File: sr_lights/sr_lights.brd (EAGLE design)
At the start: 78.4 x 64.8 mm, 33 parts, among them T1 BC847, T2 BC847, T3 BC847, T4 BC847, T5 BC847, T6 BC847, T7 BC847, T8 BC847

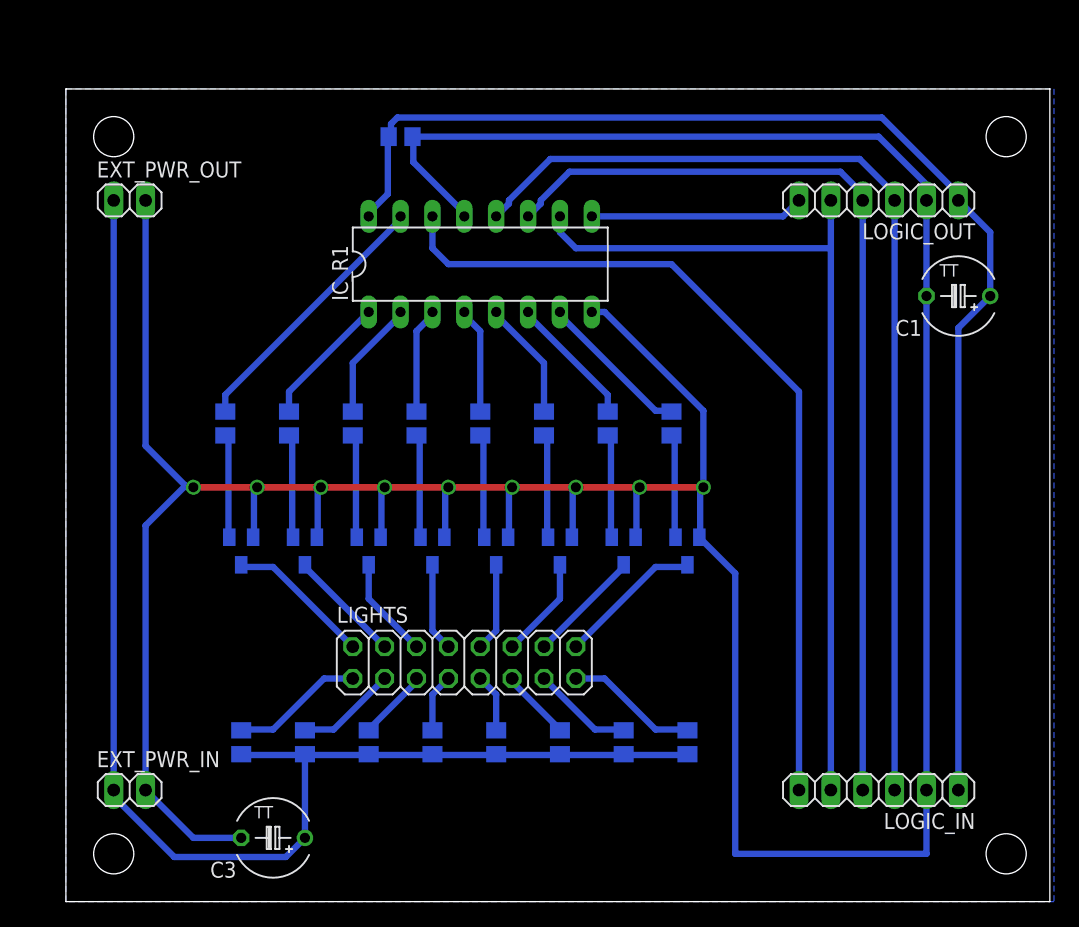
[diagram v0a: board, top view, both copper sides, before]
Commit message: DRC and align: Set the same DRC for lights and motors, fixed new DRC errors in sr_lights, aligned headers
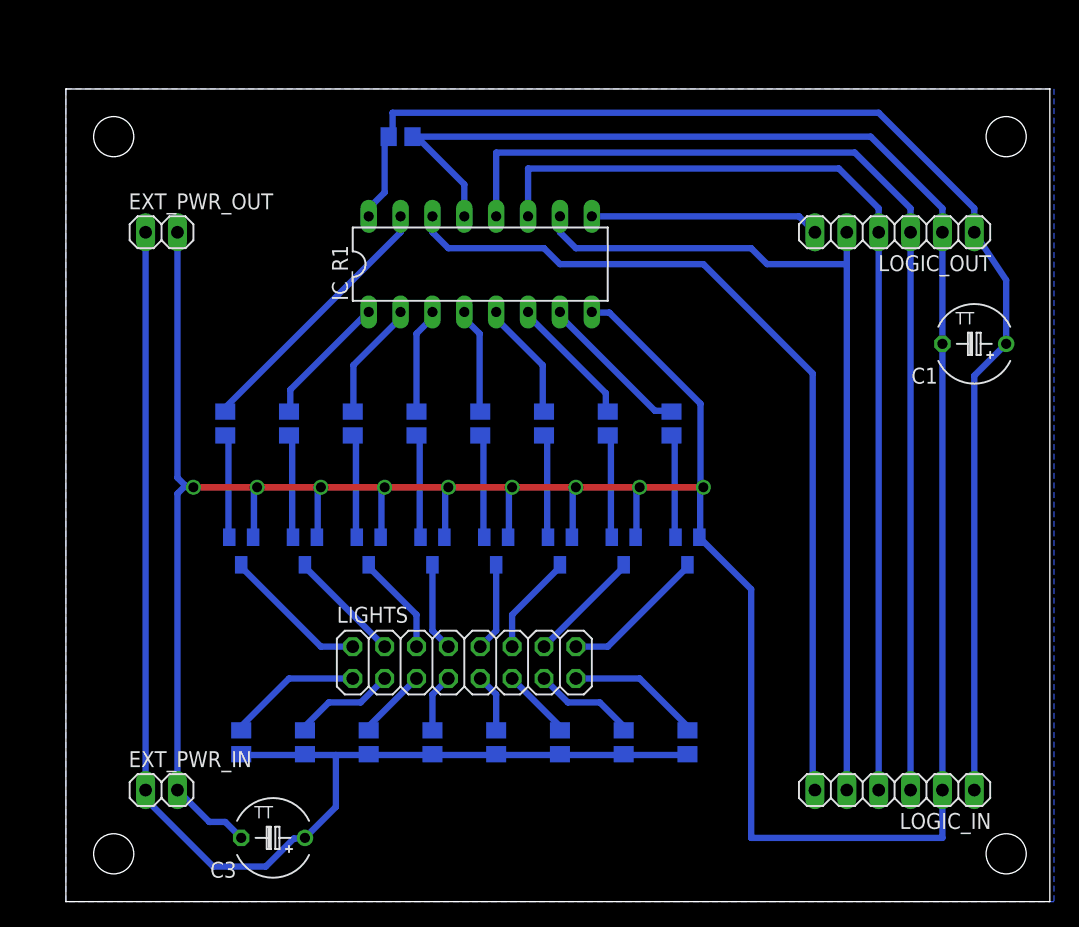
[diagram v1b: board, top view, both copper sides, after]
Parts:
- moved C1 4.02 mm to (72.4, 44.5)
- moved EXT_PWR_OUT 3.59 mm to (7.62, 53.3)
- moved LOGIC_OUT 2.84 mm to (66.0, 53.3)
- moved EXT_PWR_IN 2.54 mm to (7.62, 8.89)
- moved LOGIC_IN 1.27 mm to (66.0, 8.89)
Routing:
- net GND: track 297.9 -> 289.3 mm
- net RCK: track 82.4 -> 86.3 mm
- net VCC2: track 108.1 -> 104.7 mm
- net SCK: track 76.5 -> 79.4 mm
- net VCC1: track 105.8 -> 107.3 mm
- net SI0: track 68.2 -> 69.6 mm
- net SI1: track 17.0 -> 18.3 mm
- net SCLR: track 70.4 -> 69.5 mm

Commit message: Verion 1.2: Increased route width and board width, small other changes
Squashed commit of the following:

commit cb5b4ae53fc73325e271569d8207a4f4cb0d995e
Author: Sergey Kostyuk <contact@s-kostyuk.me>
Date:   Tue Sep 13 19:34:33 2016 +0300

    Increaded width of routes, increased board width, replaced capacitor package, updated board version

commit 30ef558f6f82cadcaf764826f9decc7df1a17ce0
Author: Sergey Kostyuk <contact@s-kostyuk.me>
Date:   Tue Sep 13 19:27:19 2016 +0300

    Replaced capacitor package

commit a2d398c50457a8d09da237926f830a1984b8064b
Author: Sergey Kostyuk <contact@s-kostyuk.me>
Date:   Tue Sep 13 18:08:38 2016 +0300

    Icreased width of routes, icreased board width

commit f5951c6459f5b93fe179c3fabd85f49e6b5260dd
Author: Sergey Kostyuk <contact@s-kostyuk.me>
Date:   Wed Sep 7 16:51:49 2016 +0300

    Increased width of power lines on sr_motors

commit 1e2f38b3539c2f4abccb8c8183ef937e4e63213c
Author: Sergey Kostyuk <ks.hot.ua@gmail.com>
Date:   Mon Aug 22 15:17:33 2016 +0300

    Added reverse current protection for external power, added version text
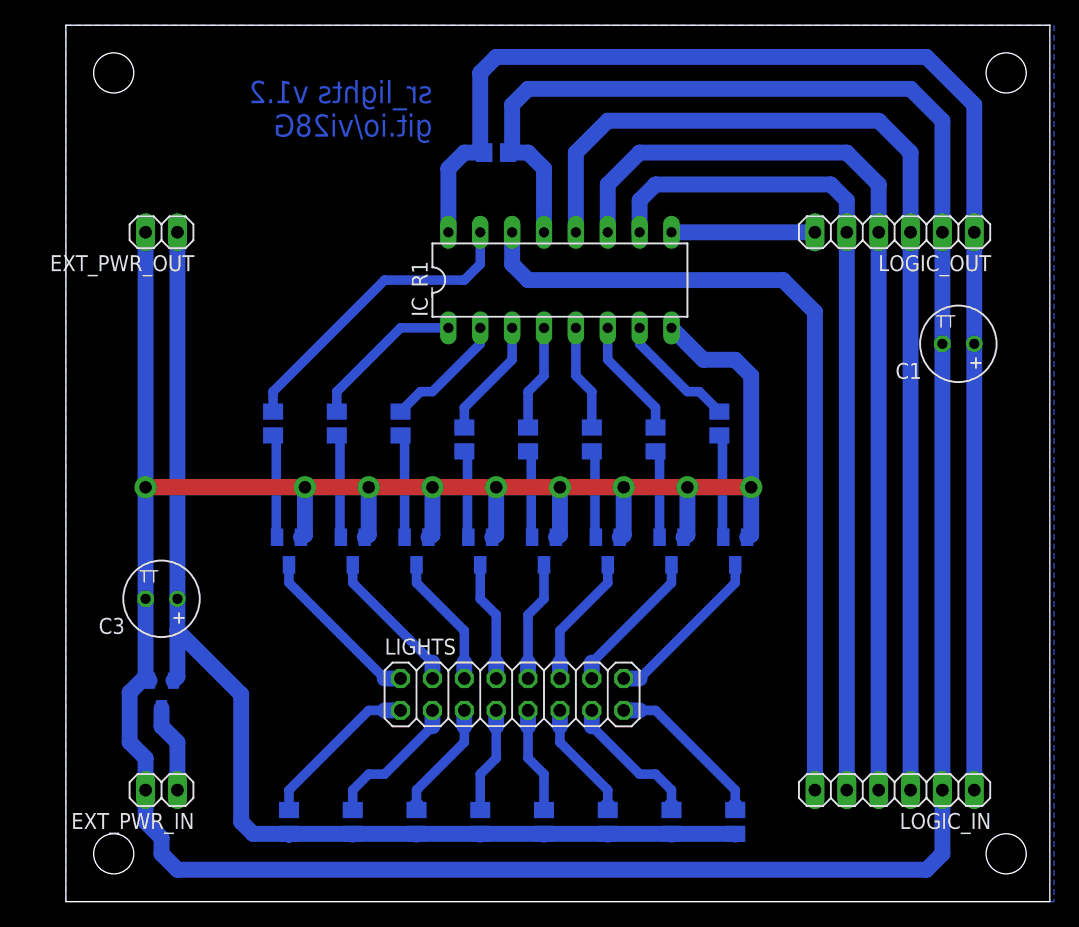
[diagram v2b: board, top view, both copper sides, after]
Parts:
- added Q1: IRLML2244TRPbF, we-transistor:SOT23
- C1, C3: device rcl:TAP5-60 -> rcl:TT2D6
- moved C3 21.0 mm to (7.62, 24.1)
- moved C2 7.73 mm to (34.3, 59.7)
- moved R3 7.41 mm to (27.9, 6.35)
- moved R4 7.41 mm to (33.0, 6.35)
- moved R5 7.41 mm to (38.1, 6.35)
- moved R6 7.41 mm to (43.2, 6.35)
- moved R8 7.41 mm to (53.3, 6.35)
- moved R1 7.41 mm to (17.8, 6.35)
- moved R2 7.41 mm to (22.9, 6.35)
- moved R7 7.41 mm to (48.3, 6.35)
- moved IC_R1 6.48 mm to (39.4, 49.5)
- moved LIGHTS 4.58 mm to (35.6, 16.5)
- moved R15 4.02 mm to (47.0, 36.8)
- moved R12 4.02 mm to (31.8, 36.8)
- moved R13 4.02 mm to (36.8, 36.8)
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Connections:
- new net VCC2_RAW: EXT_PWR_IN.1, Q1.3
- net GND: now also Q1.1
- net VCC2: now also Q1.2; no longer EXT_PWR_IN.1
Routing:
- net GND: track 289.3 -> 320.0 mm
- net VCC2: track 104.7 -> 93.5 mm
- net VCC2_RAW: track 0.00 -> 7.05 mm
- net SI1: track 18.3 -> 11.4 mm
- net N$30: track 5.71 -> 9.84 mm
- net Q0: track 21.3 -> 25.2 mm
- net N$32: track 4.66 -> 8.47 mm
- net N$21: track 5.71 -> 9.52 mm
- net N$31: track 4.66 -> 8.47 mm
- net VCC1: track 107.3 -> 111.0 mm
- net SCK: track 79.4 -> 75.8 mm
- net N$23: track 8.25 -> 11.6 mm
- net SI0: track 69.6 -> 66.3 mm
- net N$20: track 8.25 -> 11.3 mm
- net LI5: track 8.10 -> 10.8 mm
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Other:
- board size 78.4 x 64.8 mm -> 78.4 x 69.8 mm
- board text added: "sr_lights v1.2 git.io/vi28G"
